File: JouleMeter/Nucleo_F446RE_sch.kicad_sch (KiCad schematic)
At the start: 13 parts

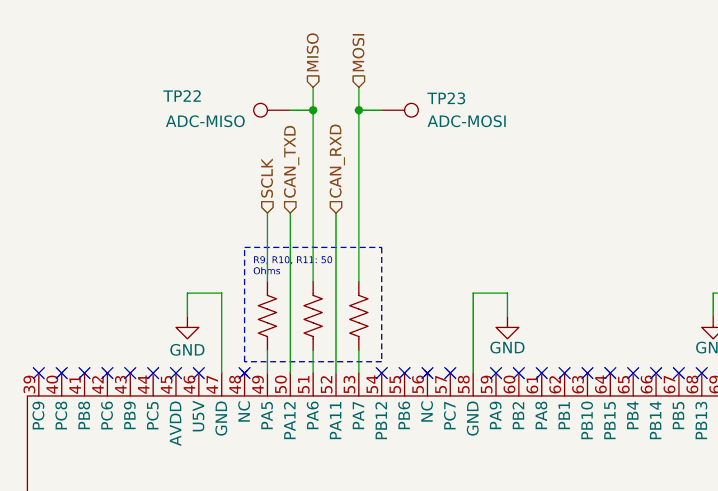
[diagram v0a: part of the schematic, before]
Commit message: Joule Meter Final
-Removed Pinnulas
-Added specific capacitor links for capacitors with a 48V across.
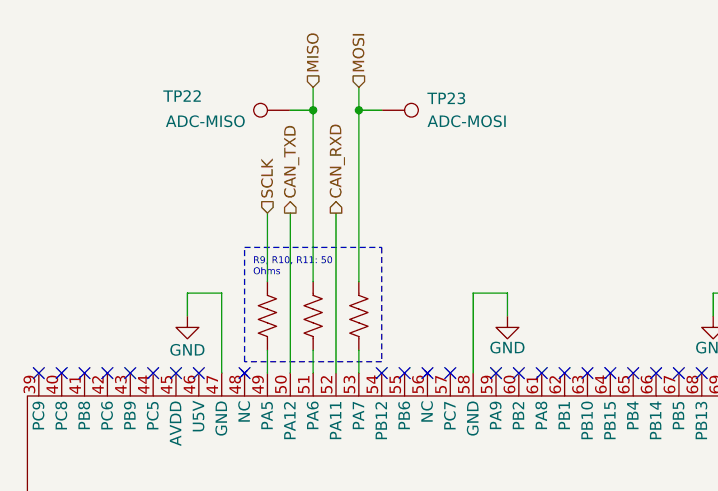
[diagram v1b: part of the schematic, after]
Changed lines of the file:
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@@
 	)
 	(hierarchical_label "CAN_TXD"
-		(shape input)
+		(shape output)
 		(at 118.11 48.26 90)
 		(effects
@@
 	)
 	(hierarchical_label "CAN_RXD"
-		(shape input)
+		(shape output)
 		(at 123.19 48.26 90)
 		(effects

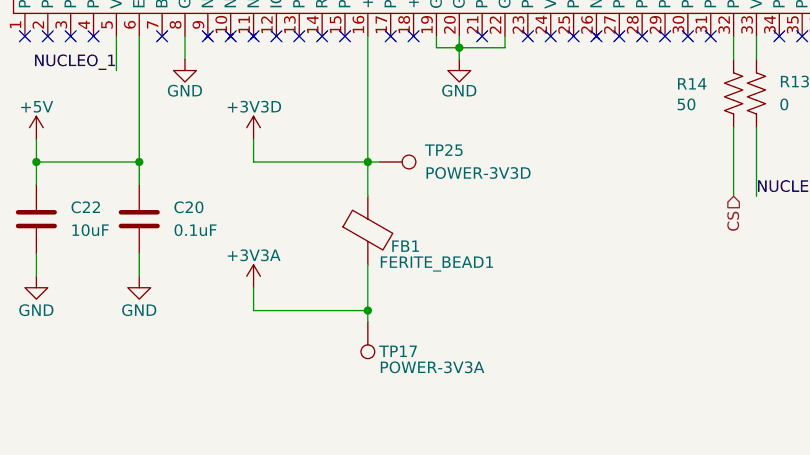
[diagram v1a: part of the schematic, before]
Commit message: added two new caps next to ferrite bead
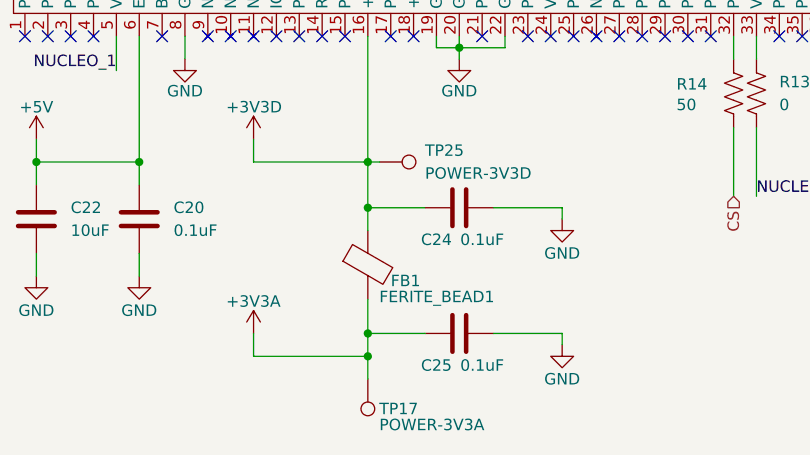
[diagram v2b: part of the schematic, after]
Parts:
- added C24, C25: 0.1uF, Capacitor_SMD:C_0805_2012Metric_Pad1.18x1.45mm_HandSolder, symbol Device:C
- Nucleo_F44RE2: value ~ -> (none)
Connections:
- net +3V3A: now also C25.1
- net +3V3D: now also C24.1
- net GND: now also C24.2, C25.2
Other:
- moved on the sheet: FERITE_BEAD1, TP17
